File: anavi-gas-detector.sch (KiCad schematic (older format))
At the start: 24 parts, among them J1 USB_B_Micro, P1 CONN_01X03, SW1 SW_DIP_x01, U1 I2C_SENS_1, U2 I2C_SENS_1, U3 I2C_SENS_1, U4 Conn_01x04, U5 Conn_01x04, U6 Conn_01x04

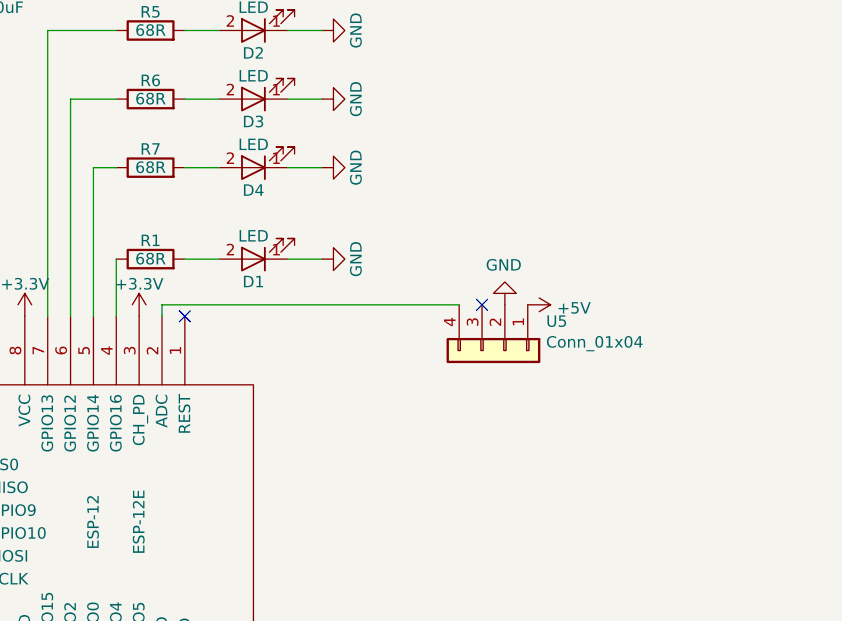
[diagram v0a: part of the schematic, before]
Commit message: anavi-gas-detector.*: Add voltage dividers
Add voltage divider to measure accrately the analog
output from the external gas sensor.

Signed-off-by: Leon Anavi <leon@anavi.org>
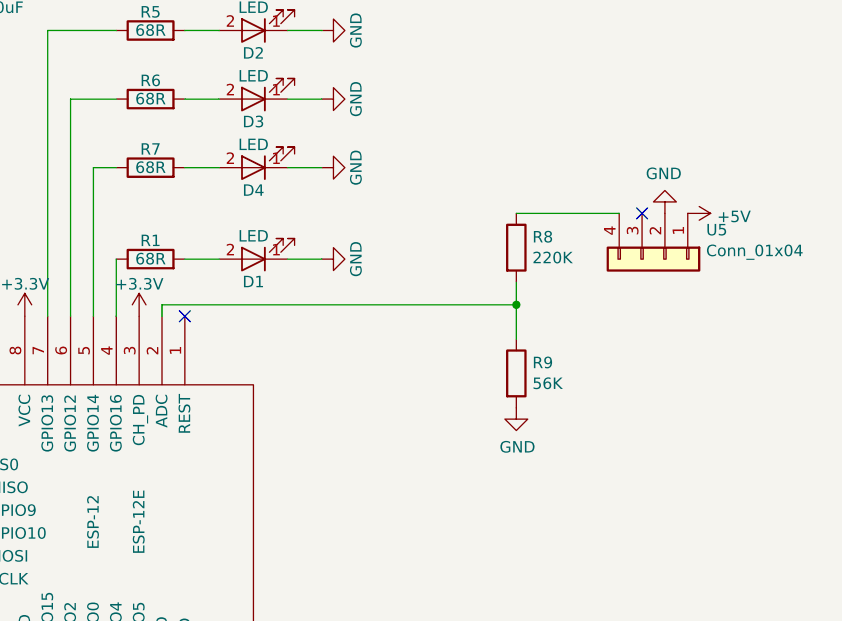
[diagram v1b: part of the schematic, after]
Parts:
- added R8: 220K, Resistor_SMD:R_0603_1608Metric, symbol Device:R
- added R9: 56K, Resistor_SMD:R_0603_1608Metric, symbol Device:R
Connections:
- net GND: now also R9.2
- net at ESP-12.2 (ADC): now also R8.2, R9.1; no longer U5.4 (Pin_4)
- new net: R8.1, U5.4 (Pin_4)
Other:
- moved on the sheet: U5
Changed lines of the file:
@@
 L Connector_Generic:Conn_01x04 U5
 U 1 1 5CAB7080
-P 4850 3450
-F 0 "U5" V 4723 3630 50  0000 L CNN
-F 1 "Conn_01x04" V 4814 3630 50  0000 L CNN
-F 2 "Connector_PinHeader_2.54mm:PinHeader_1x04_P2.54mm_Vertical" H 4850 3450 50  0001 C CNN
-F 3 "~" H 4850 3450 50  0001 C CNN
-	1    4850 3450
+P 5550 3050
+F 0 "U5" V 5423 3230 50  0000 L CNN
+F 1 "Conn_01x04" V 5514 3230 50  0000 L CNN
+F 2 "Connector_PinHeader_2.54mm:PinHeader_1x04_P2.54mm_Vertical" H 5550 3050 50  0001 C CNN
+F 3 "~" H 5550 3050 50  0001 C CNN
+	1    5550 3050
 	0    1    1    0
 $EndComp
 Wire Wire Line
 	3350 3300 3350 3250
-Wire Wire Line
-	3350 3250 4650 3250
 $Comp
 L power:+5V #PWR?
 U 1 1 5CABC645
-P 4950 3250
-F 0 "#PWR?" H 4950 3100 50  0001 C CNN
-F 1 "+5V" V 4965 3378 50  0000 L CNN
-F 2 "" H 4950 3250 50  0001 C CNN
-F 3 "" H 4950 3250 50  0001 C CNN
-	1    4950 3250
+P 5650 2850
+F 0 "#PWR?" H 5650 2700 50  0001 C CNN
+F 1 "+5V" V 5665 2978 50  0000 L CNN
+F 2 "" H 5650 2850 50  0001 C CNN
+F 3 "" H 5650 2850 50  0001 C CNN
+	1    5650 2850
 	0    1    1    0
 $EndComp
@@
 	0    1    1    0
 $EndComp
-NoConn ~ 4750 3250
+NoConn ~ 5450 2850
 $Comp
 L power:GND #PWR?
 U 1 1 5CAC01B2
-P 4850 3250
-F 0 "#PWR?" H 4850 3000 50  0001 C CNN
-F 1 "GND" H 4855 3077 50  0000 C CNN
-F 2 "" H 4850 3250 50  0001 C CNN
-F 3 "" H 4850 3250 50  0001 C CNN
-	1    4850 3250
+P 5550 2850
+F 0 "#PWR?" H 5550 2600 50  0001 C CNN
+F 1 "GND" H 5555 2677 50  0000 C CNN
+F 2 "" H 5550 2850 50  0001 C CNN
+F 3 "" H 5550 2850 50  0001 C CNN
+	1    5550 2850
 	-1   0    0    1
 $EndComp
+$Comp
+L Device:R R8
+U 1 1 5CB2C30F
+P 4900 3000
+F 0 "R8" H 4970 3046 50  0000 L CNN
+F 1 "220K" H 4970 2955 50  0000 L CNN
+F 2 "Resistor_SMD:R_0603_1608Metric" V 4830 3000 50  0001 C CNN
+F 3 "~" H 4900 3000 50  0001 C CNN
+	1    4900 3000
+	1    0    0    -1
+$EndComp
+$Comp
+L Device:R R9
+U 1 1 5CB2C3AE
+P 4900 3550
+F 0 "R9" H 4970 3596 50  0000 L CNN
+F 1 "56K" H 4970 3505 50  0000 L CNN
+F 2 "Resistor_SMD:R_0603_1608Metric" V 4830 3550 50  0001 C CNN
+F 3 "~" H 4900 3550 50  0001 C CNN
+	1    4900 3550
+	1    0    0    -1
+$EndComp
+Wire Wire Line
+	3350 3250 4900 3250
+Wire Wire Line
+	4900 3250 4900 3150
+$Comp
+L power:GND #PWR?
+U 1 1 5CB3046F
+P 4900 3700
+F 0 "#PWR?" H 4900 3450 50  0001 C CNN
+F 1 "GND" H 4905 3527 50  0000 C CNN
+F 2 "" H 4900 3700 50  0001 C CNN
+F 3 "" H 4900 3700 50  0001 C CNN
+	1    4900 3700
+	1    0    0    -1
+$EndComp
+Wire Wire Line
+	4900 2850 5350 2850
+Wire Wire Line
+	4900 3400 4900 3250
+Connection ~ 4900 3250
 $EndSCHEMATC
